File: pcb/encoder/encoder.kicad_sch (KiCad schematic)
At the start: 18 parts, among them J1 Conn_01x05, Q1 B19H1PT, Q2 B19H1PT, Q3 B19H1PT, Q4 B19H1PT, U1 LM358LV

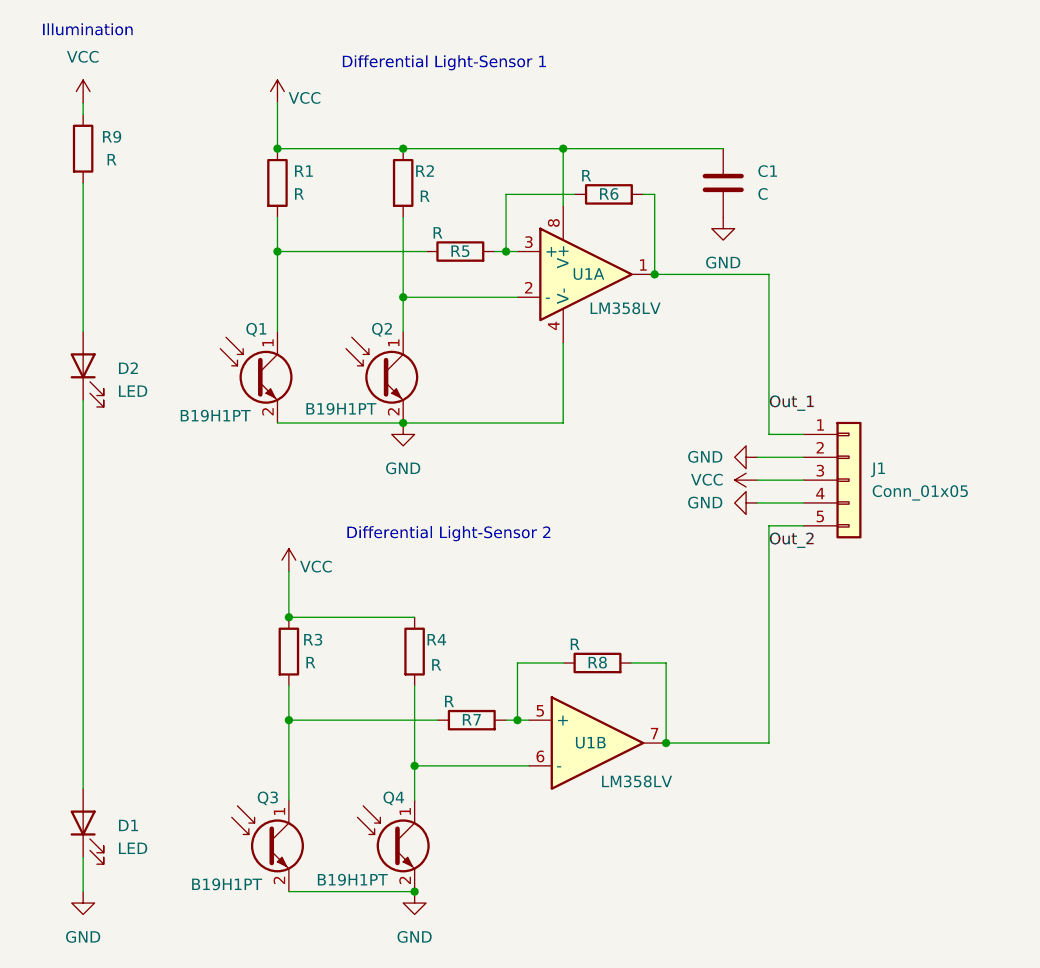
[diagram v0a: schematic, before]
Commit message: Update to separate pick-up and illumination.
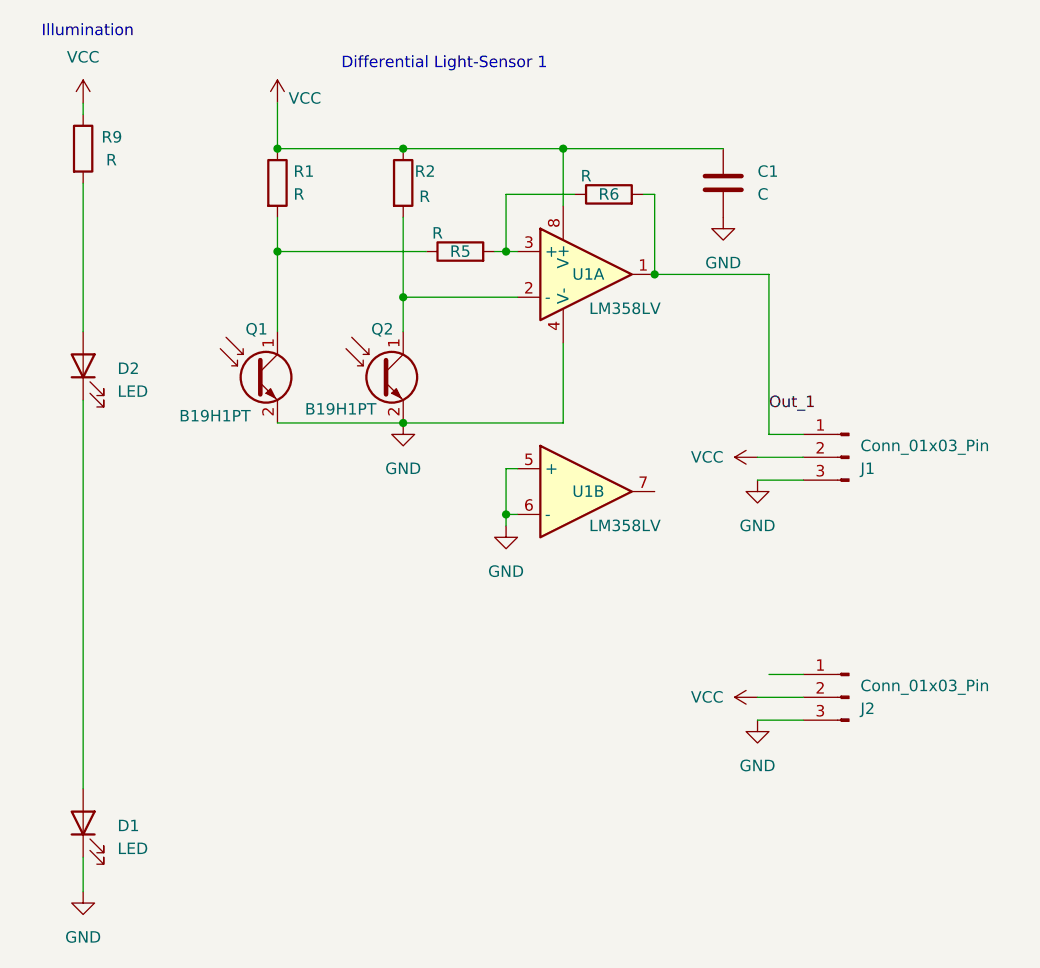
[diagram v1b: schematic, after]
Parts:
- removed J1: Conn_01x05, Connector_PinHeader_2.00mm:PinHeader_1x05_P2.00mm_Vertical, symbol Connector_Generic:Conn_01x05
- removed Q3, Q4: B19H1PT, LED_SMD:LED_0603_1608Metric, symbol Device:Q_Photo_NPN
- removed R3, R4, R7, R8: R, Resistor_SMD:R_0603_1608Metric, symbol Device:R
- added J1, J2: Conn_01x03_Pin, Connector_PinSocket_1.27mm:PinSocket_1x03_P1.27mm_Vertical, symbol Connector:Conn_01x03_Pin
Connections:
- net GND: now also U1.5 (+), U1.6 (-), J1.3 (Pin_3), J2.3 (Pin_3)
- net Out_1: now also J1.1 (Pin_1)
- net VCC: now also J1.2 (Pin_2), J2.2 (Pin_2)
- net Out_2: no longer names the net of U1.7
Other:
- note removed: "Differential Light-Sensor 2"

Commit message: Some README refinements.
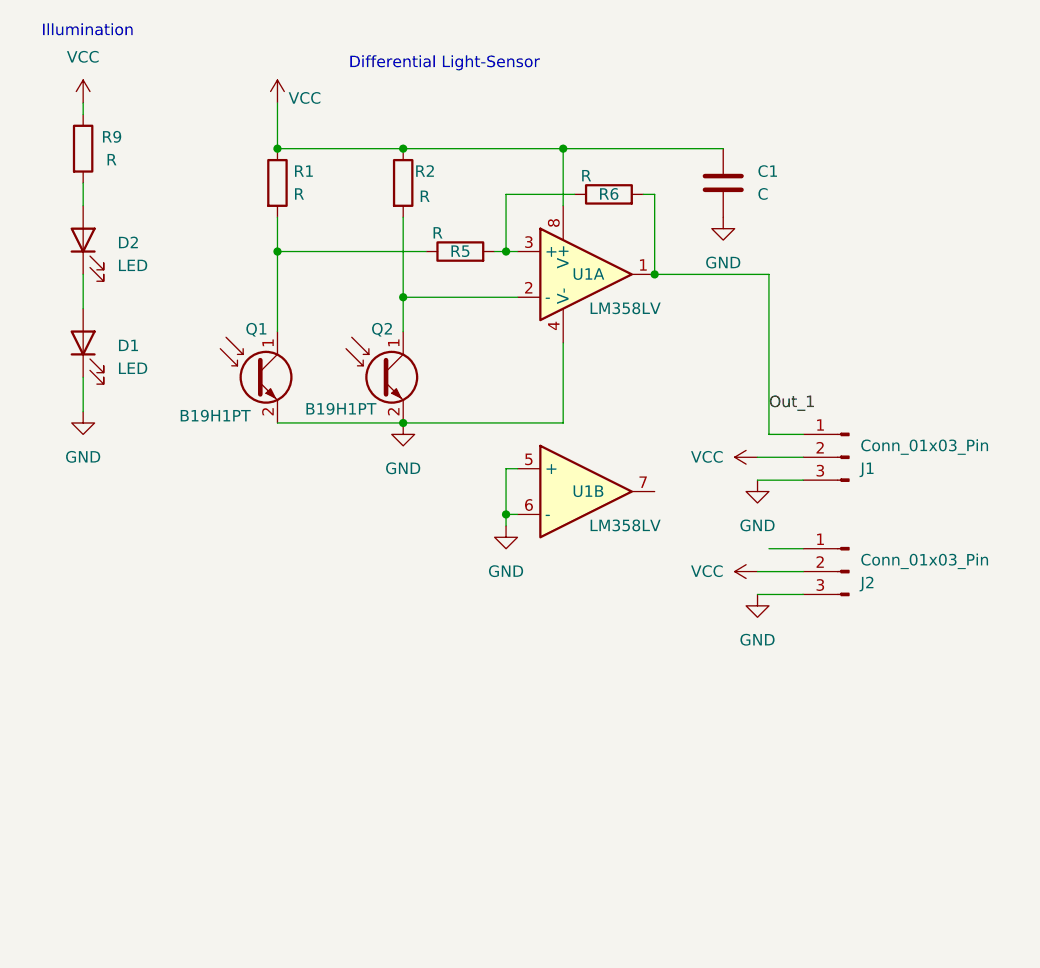
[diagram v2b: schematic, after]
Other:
- note added: "Differential Light-Sensor"
- note removed: "Differential Light-Sensor 1"
- moved on the sheet: D1, D2, J2
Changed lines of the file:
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@@
 	(wire
 		(pts
-			(xy 34.29 53.34) (xy 34.29 69.85)
+			(xy 34.29 53.34) (xy 34.29 55.88)
 		)
 		(stroke
@@
 	(wire
 		(pts
-			(xy 34.29 128.27) (xy 34.29 132.08)
-		)
-		(stroke
-			(width 0)
-			(type default)
-		)
-	)
-	(wire
-		(pts
-			(xy 110.49 107.95) (xy 114.3 107.95)
+			(xy 34.29 74.93) (xy 34.29 78.74)
+		)
+		(stroke
+			(width 0)
+			(type default)
+		)
+	)
+	(wire
+		(pts
+			(xy 110.49 93.98) (xy 114.3 93.98)
 		)
 		(stroke
@@
 	(wire
 		(pts
-			(xy 109.22 113.03) (xy 114.3 113.03)
+			(xy 109.22 99.06) (xy 114.3 99.06)
 		)
 		(stroke
@@
 	(wire
 		(pts
-			(xy 34.29 77.47) (xy 34.29 120.65)
+			(xy 34.29 63.5) (xy 34.29 67.31)
 		)
 		(stroke
@@
 	(wire
 		(pts
-			(xy 109.22 110.49) (xy 114.3 110.49)
-		)
-		(stroke
-			(width 0)
-			(type default)
-		)
-	)
-	(text "Differential Light-Sensor 1"
+			(xy 109.22 96.52) (xy 114.3 96.52)
+		)
+		(stroke
+			(width 0)
+			(type default)
+		)
+	)
+	(text "Differential Light-Sensor"
 		(exclude_from_sim no)
 		(at 74.422 40.132 0)
@@
 	(symbol
 		(lib_id "power:GND")
-		(at 109.22 113.03 0)
+		(at 109.22 99.06 0)
 		(unit 1)
 		(exclude_from_sim no)
@@
 		(dnp no)
 		(property "Reference" "#PWR09"
-			(at 109.22 119.38 0)
+			(at 109.22 105.41 0)
 			(effects
 				(font
@@
 		)
 		(property "Value" "GND"
-			(at 109.22 118.11 0)
+			(at 109.22 104.14 0)
 			(effects
 				(font
@@
 		)
 		(property "Footprint" ""
-			(at 109.22 113.03 0)
+			(at 109.22 99.06 0)
 			(effects
 				(font
@@
 		)
 		(property "Datasheet" ""
-			(at 109.22 113.03 0)
+			(at 109.22 99.06 0)
 			(effects
 				(font
@@
 		)
 		(property "Description" "Power symbol creates a global label with name \"GND\" , ground"
-			(at 109.22 113.03 0)
+			(at 109.22 99.06 0)
 			(effects
 				(font
@@
 	(symbol
 		(lib_id "power:VCC")
-		(at 109.22 110.49 90)
+		(at 109.22 96.52 90)
 		(unit 1)
 		(exclude_from_sim no)
@@
 		(dnp no)
 		(property "Reference" "#PWR06"
-			(at 113.03 110.49 0)
+			(at 113.03 96.52 0)
 			(effects
 				(font
@@
 		)
 		(property "Value" "VCC"
-			(at 103.632 110.49 90)
+			(at 103.632 96.52 90)
 			(effects
 				(font
@@
 		)
 		(property "Footprint" ""
-			(at 109.22 110.49 0)
+			(at 109.22 96.52 0)
 			(effects
 				(font
@@
 		)
 		(property "Datasheet" ""
-			(at 109.22 110.49 0)
+			(at 109.22 96.52 0)
 			(effects
 				(font
@@
 		)
 		(property "Description" "Power symbol creates a global label with name \"VCC\""
-			(at 109.22 110.49 0)
+			(at 109.22 96.52 0)
 			(effects
 				(font
@@
 	(symbol
 		(lib_id "Device:LED")
-		(at 34.29 124.46 90)
+		(at 34.29 71.12 90)
 		(unit 1)
 		(exclude_from_sim no)
@@
 		(fields_autoplaced yes)
 		(property "Reference" "D1"
-			(at 38.1 124.7774 90)
+			(at 38.1 71.4374 90)
 			(effects
 				(font
@@
 		)
 		(property "Value" "LED"
-			(at 38.1 127.3174 90)
+			(at 38.1 73.9774 90)
 			(effects
 				(font
@@
 		)
 		(property "Footprint" "LED_SMD:LED_0603_1608Metric"
-			(at 34.29 124.46 0)
+			(at 34.29 71.12 0)
 			(effects
 				(font
@@
 		)
 		(property "Datasheet" "~"
-			(at 34.29 124.46 0)
+			(at 34.29 71.12 0)
 			(effects
 				(font
@@
 		)
 		(property "Description" "Light emitting diode"
-			(at 34.29 124.46 0)
+			(at 34.29 71.12 0)
 			(effects
 				(font
@@
 	(symbol
 		(lib_id "Connector:Conn_01x03_Pin")
-		(at 119.38 110.49 0)
+		(at 119.38 96.52 0)
 		(mirror y)
 		(unit 1)
@@
 		(dnp no)
 		(property "Reference" "J2"
-			(at 120.65 111.7601 0)
+			(at 120.65 97.7901 0)
 			(effects
 				(font
@@
 		)
 		(property "Value" "Conn_01x03_Pin"
-			(at 120.65 109.2201 0)
+			(at 120.65 95.2501 0)
 			(effects
 				(font
@@
 		)
 		(property "Footprint" "Connector_PinSocket_1.27mm:PinSocket_1x03_P1.27mm_Vertical"
-			(at 119.38 110.49 0)
+			(at 119.38 96.52 0)
 			(effects
 				(font
@@
 		)
 		(property "Datasheet" "~"
-			(at 119.38 110.49 0)
+			(at 119.38 96.52 0)
 			(effects
 				(font
@@
 		)
 		(property "Description" "Generic connector, single row, 01x03, script generated"
-			(at 119.38 110.49 0)
+			(at 119.38 96.52 0)
 			(effects
 				(font
@@
 	(symbol
 		(lib_id "power:GND")
-		(at 34.29 132.08 0)
+		(at 34.29 78.74 0)
 		(unit 1)
 		(exclude_from_sim no)
@@
 		(fields_autoplaced yes)
 		(property "Reference" "#PWR01"
-			(at 34.29 138.43 0)
+			(at 34.29 85.09 0)
 			(effects
 				(font
@@
 		)
 		(property "Value" "GND"
-			(at 34.29 137.16 0)
+			(at 34.29 83.82 0)
 			(effects
 				(font
@@
 		)
 		(property "Footprint" ""
-			(at 34.29 132.08 0)
+			(at 34.29 78.74 0)
 			(effects
 				(font
@@
 		)
 		(property "Datasheet" ""
-			(at 34.29 132.08 0)
+			(at 34.29 78.74 0)
 			(effects
 				(font
@@
 		)
 		(property "Description" "Power symbol creates a global label with name \"GND\" , ground"
-			(at 34.29 132.08 0)
+			(at 34.29 78.74 0)
 			(effects
 				(font
@@
 	(symbol
 		(lib_id "Device:LED")
-		(at 34.29 73.66 90)
+		(at 34.29 59.69 90)
 		(unit 1)
 		(exclude_from_sim no)
@@
 		(fields_autoplaced yes)
 		(property "Reference" "D2"
-			(at 38.1 73.9774 90)
+			(at 38.1 60.0074 90)
 			(effects
 				(font
@@
 		)
 		(property "Value" "LED"
-			(at 38.1 76.5174 90)
+			(at 38.1 62.5474 90)
 			(effects
 				(font
@@
 		)
 		(property "Footprint" "LED_SMD:LED_0603_1608Metric"
-			(at 34.29 73.66 0)
+			(at 34.29 59.69 0)
 			(effects
 				(font
@@
 		)
 		(property "Datasheet" "~"
-			(at 34.29 73.66 0)
+			(at 34.29 59.69 0)
 			(effects
 				(font
@@
 		)
 		(property "Description" "Light emitting diode"
-			(at 34.29 73.66 0)
-			(effects
-				(font
+			(at 34.29 59.69 0)
+			(effects
+				(font
